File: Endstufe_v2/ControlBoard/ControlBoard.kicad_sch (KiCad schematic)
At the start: 7 parts, among them J1 B4B-XH-2_(LF)(SN), J15 B4B-XH-2_(LF)(SN), J16 B6B-XH-2(LF)(SN), J2 B4B-XH-2_(LF)(SN), J3 B4B-XH-2_(LF)(SN), J4 DNP, J5 B6B-XH-2(LF)(SN)

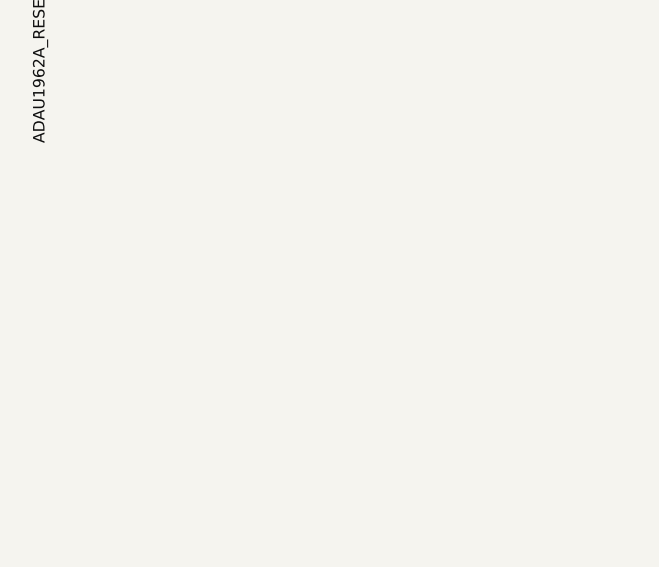
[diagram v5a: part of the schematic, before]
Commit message: Make mounting holes and continue layouting
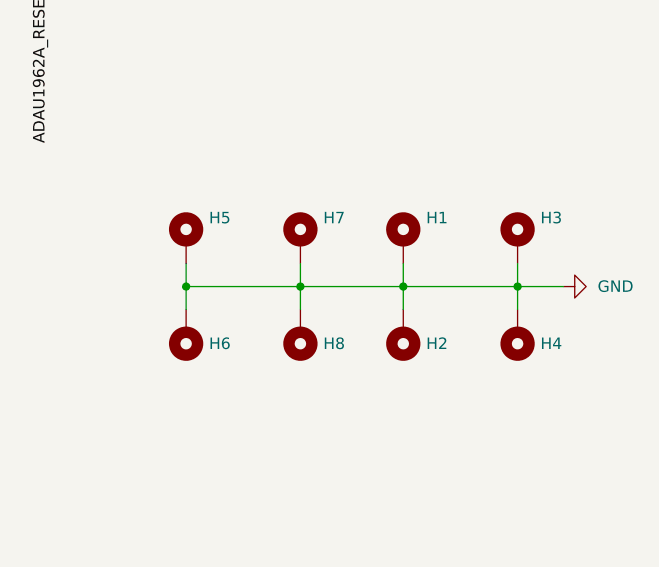
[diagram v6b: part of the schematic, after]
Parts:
- added H1, H2, H3, H4, H5, H6, H7, H8: MountingHole_Pad, Endstufe:MountingHole_3.2mm_M3_ISO14580_Pad, symbol Endstufe:MountingHole_Pad
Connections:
- net GND: now also H1.1, H2.1, H3.1, H4.1, H5.1, H6.1, H7.1, H8.1

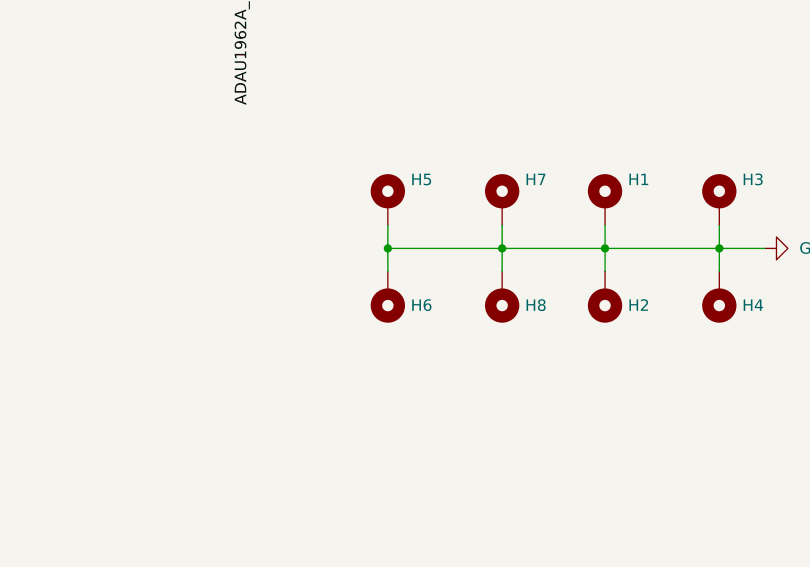
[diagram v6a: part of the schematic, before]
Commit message: Finish layout of control and input board for now
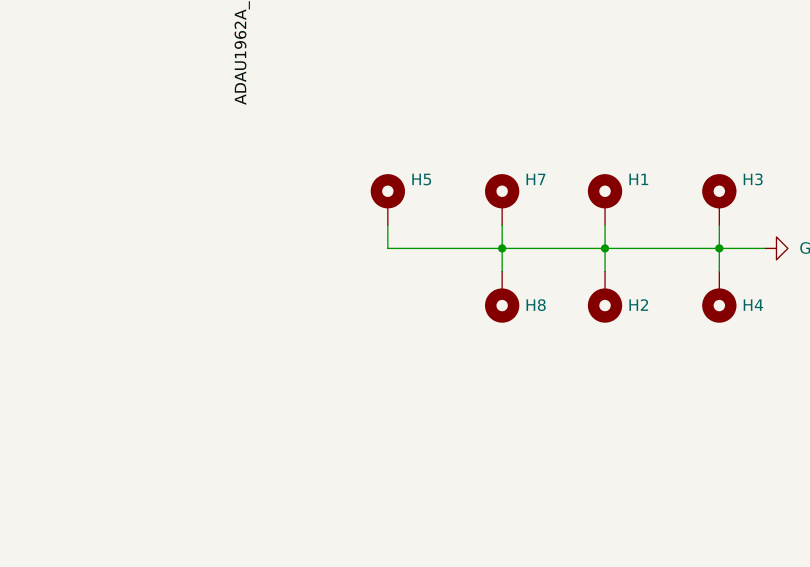
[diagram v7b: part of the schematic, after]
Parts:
- removed H6: MountingHole_Pad, Endstufe:MountingHole_3.2mm_M3_ISO14580_Pad, symbol Endstufe:MountingHole_Pad
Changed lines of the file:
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@@
-	)
-	(junction
-		(at 209.55 142.24)
-		(diameter 0)
-		(color 0 0 0 0)
 	)
 	(junction
@@
 		(pts
 			(xy 143.51 45.72) (xy 177.8 45.72)
-		)
-		(stroke
-			(width 0)
-			(type default)
-		)
-	)
-	(wire
-		(pts
-			(xy 209.55 142.24) (xy 209.55 144.78)
 		)
 		(stroke
@@
 					(unit 1)
 				)
-			)
-		)
-	)
-	(symbol
-		(lib_id "Endstufe:MountingHole_Pad")
-		(at 209.55 147.32 180)
-		(unit 1)
-		(exclude_from_sim no)
-		(in_bom yes)
-		(on_board yes)
-		(dnp no)
-		(fields_autoplaced yes)
-		(property "Reference" "H6"
-			(at 212.09 148.5899 0)
-			(effects
-				(font
-					(size 1.27 1.27)
-				)
-				(justify right)
-			)
-		)
-		(property "Value" "MountingHole_Pad"
-			(at 207.01 147.3201 0)
-			(effects
-				(font
-					(size 1.27 1.27)
-				)
-				(justify left)
-				(hide yes)
-			)
-		)
-		(property "Footprint" "Endstufe:MountingHole_3.2mm_M3_ISO14580_Pad"
-			(at 209.55 147.32 0)
-			(effects
-				(font
-					(size 1.27 1.27)
-				)
-				(hide yes)
-			)
-		)
-		(property "Datasheet" "~"
-			(at 209.55 147.32 0)
-			(effects
-				(font
-					(size 1.27 1.27)
-				)
-				(hide yes)
-			)
-		)
-		(property "Description" "Mounting Hole with connection"
-			(at 209.55 147.32 0)
-			(effects
-				(font
-					(size 1.27 1.27)
-				)
-				(hide yes)
-			)
-		)
-		(pin "1"
-		)
-		(instances
-			(project "ControlBoard"
-				(path "/4f887f51-77c1-41d4-a3eb-45d362caffe1"
-					(reference "H6")
-					(unit 1)
-				)

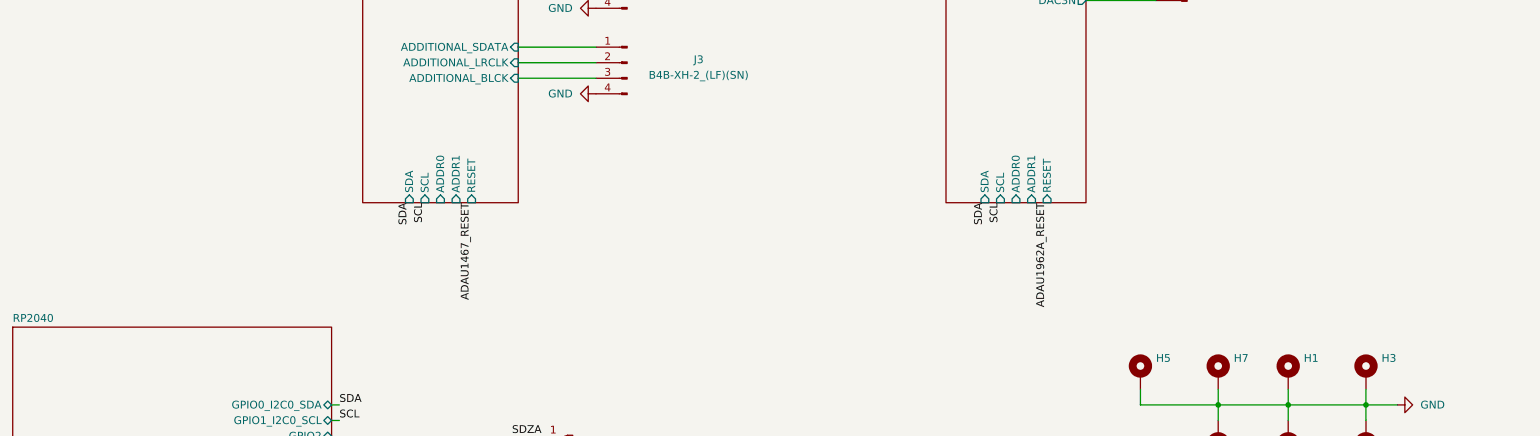
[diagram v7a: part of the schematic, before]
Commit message: Add missing I2C adress headers and pull down for DAC and DSP
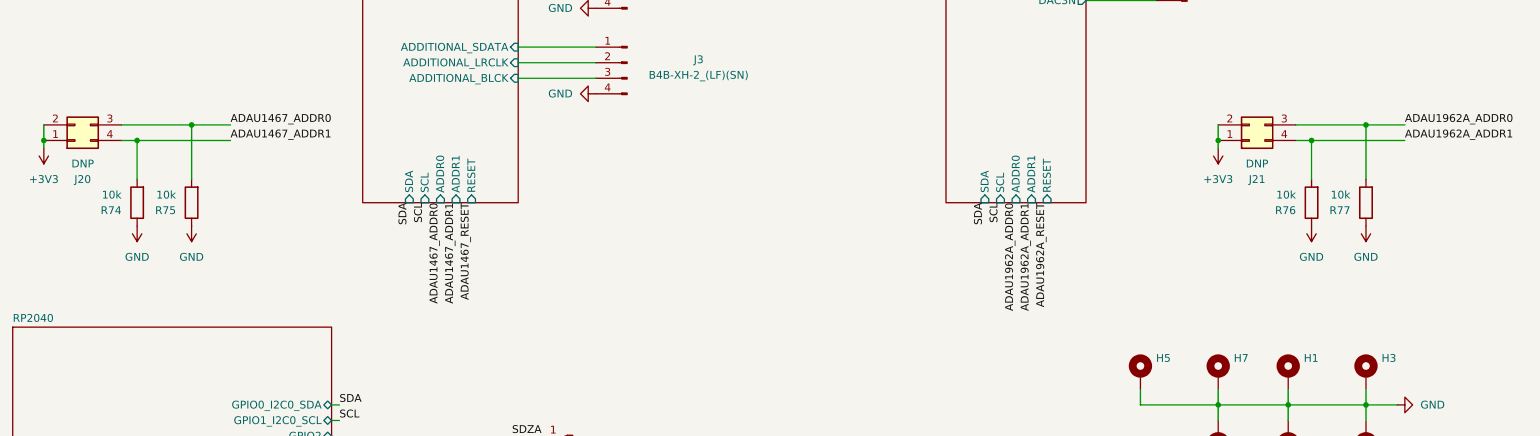
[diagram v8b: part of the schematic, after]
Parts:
- added J20, J21: DNP, Connector_PinHeader_2.54mm:PinHeader_2x02_P2.54mm_Vertical, symbol Connector_Generic:Conn_02x02_Counter_Clockwise
- added R74, R75, R76, R77: 10k, Endstufe:C_0402_1005Metric, symbol Endstufe:R
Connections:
- net GND: now also R74.1, R75.1, R76.1, R77.1
- new net +3V3: J20.1 (Pin_1), J20.2 (Pin_2), J21.1 (Pin_1), J21.2 (Pin_2)
- new net ADAU1467_ADDR0: J20.3 (Pin_3), R75.2
- new net ADAU1467_ADDR1: J20.4 (Pin_4), R74.2
- new net ADAU1962A_ADDR0: J21.3 (Pin_3), R77.2
- new net ADAU1962A_ADDR1: J21.4 (Pin_4), R76.2
